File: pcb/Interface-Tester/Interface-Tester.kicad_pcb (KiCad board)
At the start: 2 copper layers, 62.8 x 18.5 mm, 17 parts, among them J1 INTERFACE, J2 I2C, J3 PWR, SW1 SW, SW2 SW, SW3 SW, SW4 SW, SW5 SW, SW6 SW, SW7 SW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

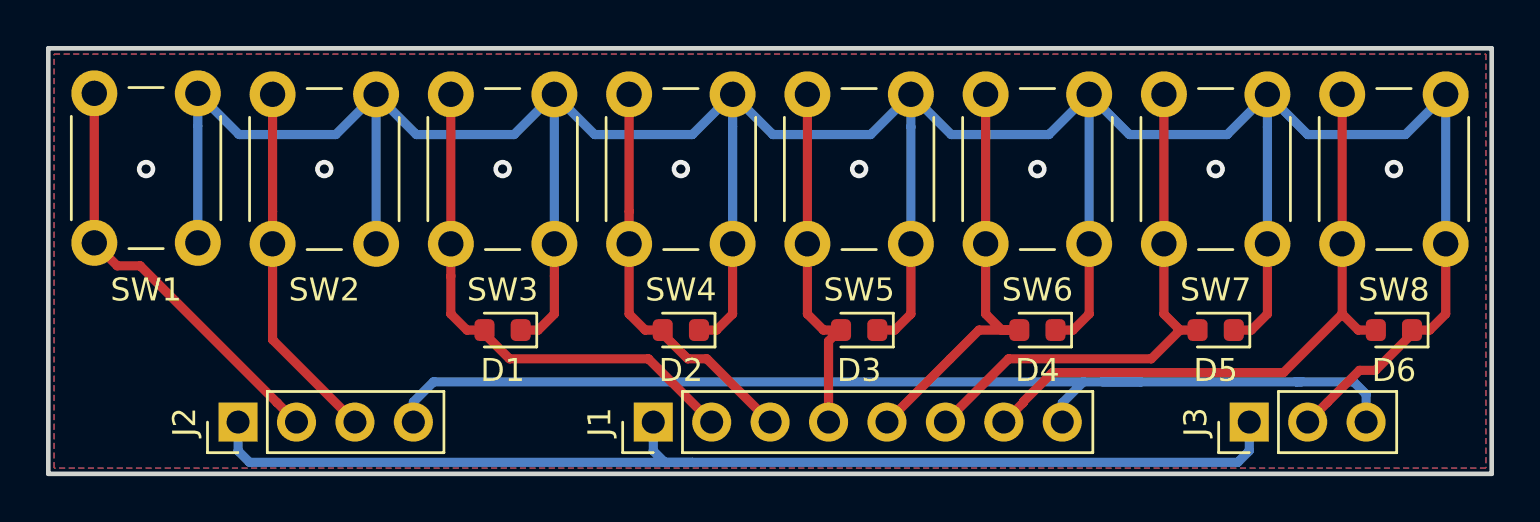
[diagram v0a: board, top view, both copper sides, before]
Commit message: Upgrade Interface Tester to KiCad 6.0
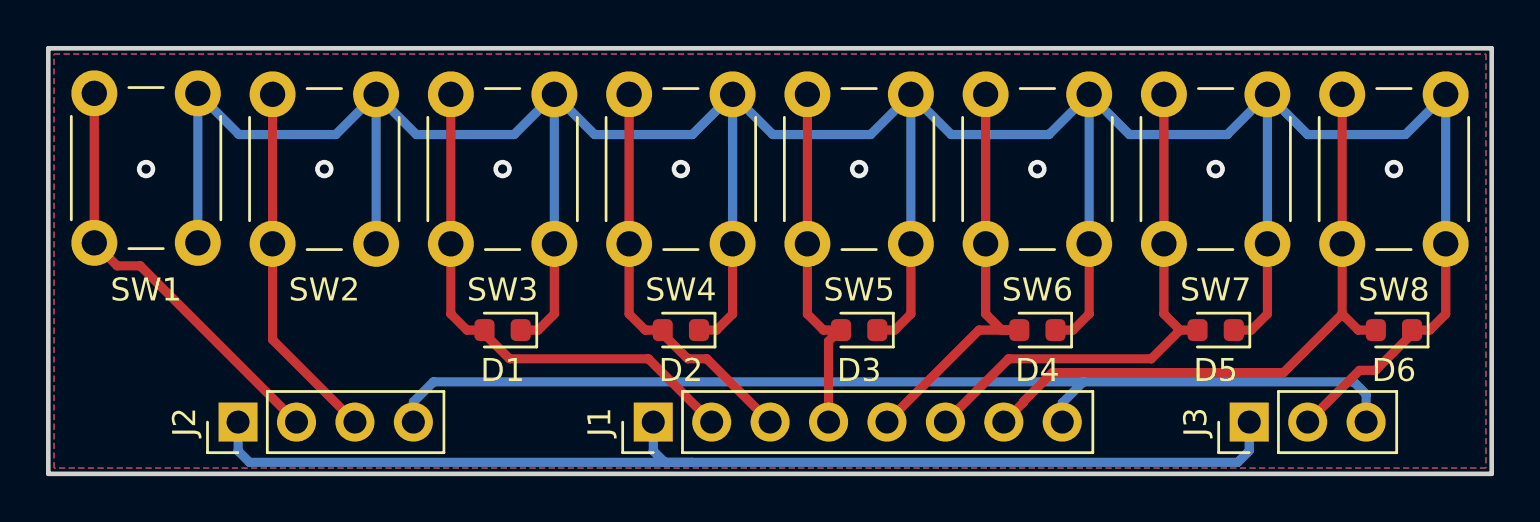
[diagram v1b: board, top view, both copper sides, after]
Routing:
- net +3V3: track 48.1 -> 46.2 mm
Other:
- net class Default removed
- board text added: "BasilFX 09/2022 V1.2.0"
- board text removed: "BasilFX 08/2018 V1.1.0"
